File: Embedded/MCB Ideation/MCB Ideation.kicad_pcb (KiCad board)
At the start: 2 copper layers, 19.8 x 26.8 mm, 22 parts, among them J1 MSD-1-A, U1 ICM-20948, U2 BME280, U3 USB, U4 AP7366-33W5-7

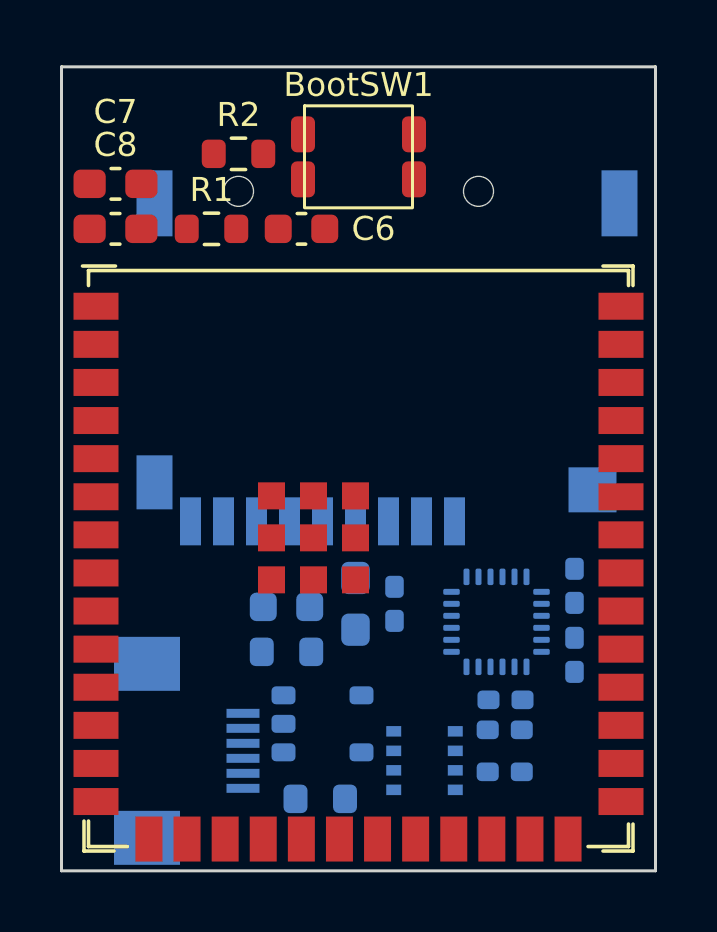
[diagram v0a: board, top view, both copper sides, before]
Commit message: Ideation PCB Component Compaction
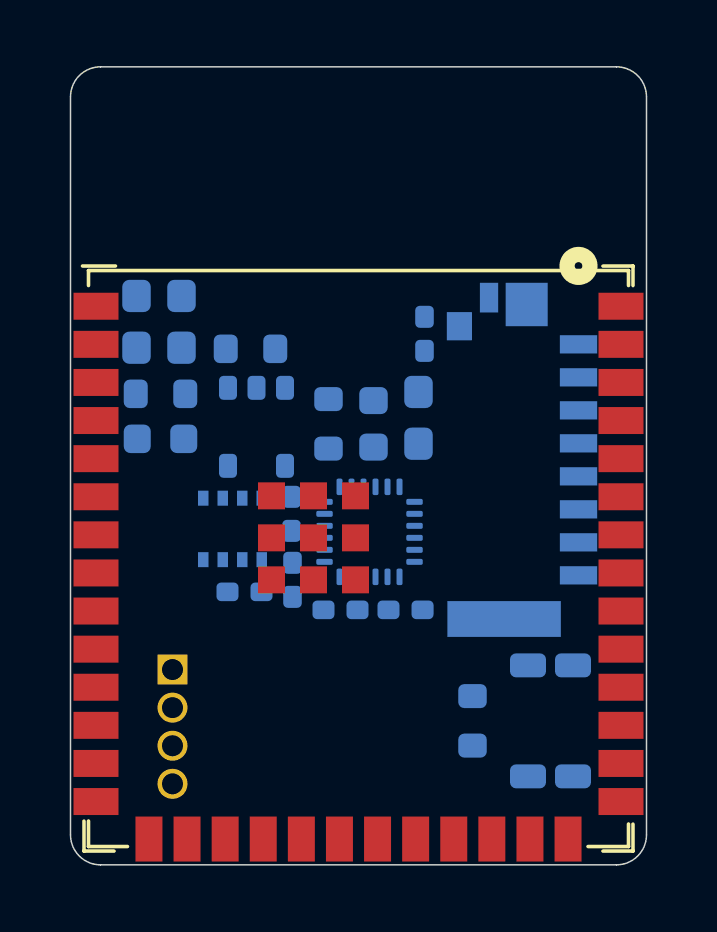
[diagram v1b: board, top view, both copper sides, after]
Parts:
- removed J1: MSD-1-A, MicroSD_MSD_1_A:CUI_MSD-1-A
- removed U3: USB, FFC_Connector:FFC Aliexpress 0.5mm 6P
- added J2: USB, Connector_PinSocket_1.27mm:PinSocket_1x04_P1.27mm_Vertical, B.Cu at (133.8, 103.4)
- added J3: MicroSD, MicroSD_473092651:CONN12_47309-2651_MOL, B.Cu at (145.9, 96.4)
- BootSW1, C6, C7, C8, R1, R2: moved to B.Cu
- moved R2 20.4 mm to (143.8, 105.1), turned to -90 degrees
- moved BootSW1 19.9 mm to (146.4, 105.1), turned to 90 degrees
- moved C11 15.2 mm to (136.4, 92.7)
- moved C4 10.5 mm to (136.2, 100.8)
- moved U4 10.1 mm to (136.6, 95.3), turned to 180 degrees
- moved U2 10.0 mm to (135.8, 98.7), turned to 180 degrees
- moved C2 9.45 mm to (137.8, 98.2), turned to 90 degrees
- moved C10 9.06 mm to (142.2, 92.2), turned to 90 degrees
- moved C5 8.66 mm to (137.8, 100.4), turned to -90 degrees
- moved C6 8.43 mm to (133.4, 95.7)
- moved C3 7.94 mm to (139.4, 101.4), turned to 180 degrees
- moved C12 7.73 mm to (139.0, 95.2), turned to 90 degrees
- moved C13 6.75 mm to (140.5, 95.2), turned to 90 degrees
- moved C9 6.55 mm to (142.0, 95.0)
- moved R1 5.76 mm to (133.4, 94.2), turned to 180 degrees
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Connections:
- ESP1 pad 10: GPS Reset -> unconnected-(ESP1-GPIO17/U1TXD/ADC2_CH6-Pad10)
- ESP1 pad 11: 3V3 Jaw LEDS -> unconnected-(ESP1-GPIO18/U1RXD/ADC2_CH7/CLK_OUT3-Pad11)
- ESP1 pad 17: GPS UART TX -> unconnected-(ESP1-GPIO9/TOUCH9/ADC1_CH8/FSPIHD/SUBSPIHD-Pad17)
- ESP1 pad 18: GPS UART RX -> unconnected-(ESP1-GPIO10/TOUCH10/ADC1_CH9/FSPICS0/FSPIIO4/SUBSPICS0-Pad18)
- ESP1 pad 19: SDA -> unconnected-(ESP1-GPIO11/TOUCH11/ADC2_CH0/FSPID/FSPIIO5/SUBSPID-Pad19)
- ESP1 pad 20: SCL -> unconnected-(ESP1-GPIO12/TOUCH12/ADC2_CH1/FSPICLK/FSPIIO6/SUBSPICLK-Pad20)
- ESP1 pad 21: CPU-PDU SCL -> unconnected-(ESP1-GPIO13/TOUCH13/ADC2_CH2/FSPIQ/FSPIIO7/SUBSPIQ-Pad21)
- ESP1 pad 22: CPU-PDU SDA -> unconnected-(ESP1-GPIO14/TOUCH14/ADC2_CH3/FSPIWP/FSPIDQS/SUBSPIWP-Pad22)
- ESP1 pad 23: CPU-Mask RX -> unconnected-(ESP1-GPIO21-Pad23)
- ESP1 pad 24: CPU-Mask TX -> unconnected-(ESP1-GPIO47/SPICLK_P/SUBSPICLK_P_DIFF-Pad24)
- ESP1 pad 28: CPU-GPU GPIO 2 -> unconnected-(ESP1-SPIIO6/GPIO35/FSPID/SUBSPID-Pad28)
- ESP1 pad 29: CPU-GPU GPIO 3 -> unconnected-(ESP1-SPIIO7/GPIO36/FSPICLK/SUBSPICLK-Pad29)
- ESP1 pad 30: CPU-GPU TX -> unconnected-(ESP1-SPIDQS/GPIO37/FSPIQ/SUBSPIQ-Pad30)
- ESP1 pad 31: CPU-GPU RX -> unconnected-(ESP1-GPIO38/FSPIWP/SUBSPIWP-Pad31)
- ESP1 pad 32: CPU-GPU GPIO 1 -> unconnected-(ESP1-MTCK/GPIO39/CLK_OUT3/SUBSPICS1-Pad32)
- ESP1 pad 33: CPU-GPU GPIO 0 -> unconnected-(ESP1-MTDO/GPIO40/CLK_OUT2-Pad33)
- ESP1 pad 34: CPU-Mask GPIO 1 -> unconnected-(ESP1-MTDI/GPIO41/CLK_OUT1-Pad34)
- ESP1 pad 35: CPU-Mask GPIO 0 -> unconnected-(ESP1-MTMS/GPIO42-Pad35)
- ESP1 pad 4: 3V3 Neck LEDS -> unconnected-(ESP1-GPIO4/TOUCH4/ADC1_CH3-Pad4)
- ESP1 pad 5: SD Card CS -> unconnected-(ESP1-GPIO5/TOUCH5/ADC1_CH4-Pad5)
- ESP1 pad 6: SD Card MOSI -> unconnected-(ESP1-GPIO6/TOUCH6/ADC1_CH5-Pad6)
- ESP1 pad 7: SD Card CLK -> unconnected-(ESP1-GPIO7/TOUCH7/ADC1_CH6-Pad7)
- ESP1 pad 8: SD Card MISO -> unconnected-(ESP1-GPIO15/U0RTS/ADC2_CH4/XTAL_32K_P-Pad8)
- ESP1 pad 9: SD Card Detect -> unconnected-(ESP1-GPIO16/U0CTS/ADC2_CH5/XTAL_32K_N-Pad9)
- U1 pad 23: SCL -> /SCL
- U1 pad 24: SDA -> /SDA
- U2 pad 3: SDA -> /SDA
- U2 pad 4: SCL -> /SCL
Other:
- board size 19.8 x 26.8 mm -> 19.2 x 26.6 mm
